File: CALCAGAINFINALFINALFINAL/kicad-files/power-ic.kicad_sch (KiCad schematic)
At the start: 18 parts, among them J2 USB_C_Receptacle_USB2.0_16P, SW10 SW_SPST, U5 TP4056-42-ESOP8, U6 TLV61070ADBV

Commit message: added 11pin expansion for accessories and micro-sd card slot
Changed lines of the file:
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@@
-		)
-	)
-	(label "VCC"
-		(at 77.216 62.23 0)
-		(effects
-			(font
-				(size 1.27 1.27)
-			)
-			(justify left bottom)
 		)
 	)
@@
 				(hide yes)
 			)
+		)
+	)
+	(global_label "VCC"
+		(shape input)
+		(at 77.216 62.23 0)
+		(fields_autoplaced yes)
+		(effects
+			(font
+				(size 1.27 1.27)
+			)
+			(justify left)
+		)
+		(property "Intersheetrefs" "${INTERSHEET_REFS}"
+			(at 83.8298 62.23 0)
+			(effects
+				(font
+					(size 1.27 1.27)
+				)
+				(justify left)
+				(hide yes)
+			)

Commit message: Finished SD card and screen. Added camera connector and adjacent gpio expander
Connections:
- net GND: now also J2.S1 (SHIELD)
- no-connect marks 3 -> 2
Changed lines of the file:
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@@
 		(at 77.216 90.17)
-	)
-	(no_connect
-		(at 54.356 100.33)
 	)
 	(wire
@@
 			(effects
 				(font
+					(size 1.27 1.27)
+				)
+				(justify right)
+				(hide yes)
+			)
+		)
+	)
+	(global_label "GND"
+		(shape input)
+		(at 54.356 100.33 270)
+		(fields_autoplaced yes)
+		(effects
+			(font
+				(size 1.27 1.27)
+			)
+			(justify right)
+		)
+		(property "Intersheetrefs" "${INTERSHEET_REFS}"
+			(at 54.356 107.1857 90)
+			(effects
+				(font

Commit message: nearly finished with the no camera variant schematic stil have 2 drc warnings to fix but should be done in the next few hours.
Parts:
- removed BT2: BAT, symbol Device:Battery_Cell
- added H6, H7: MountingHole_Pad, MountingHole:MountingHole_2.7mm_M2.5_ISO7380_Pad, symbol Mechanical:MountingHole_Pad
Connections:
- net BAT+: now also H7.1
- net GND: now also J2.SH (SHIELD), H6.1; no longer J2.S1 (SHIELD)

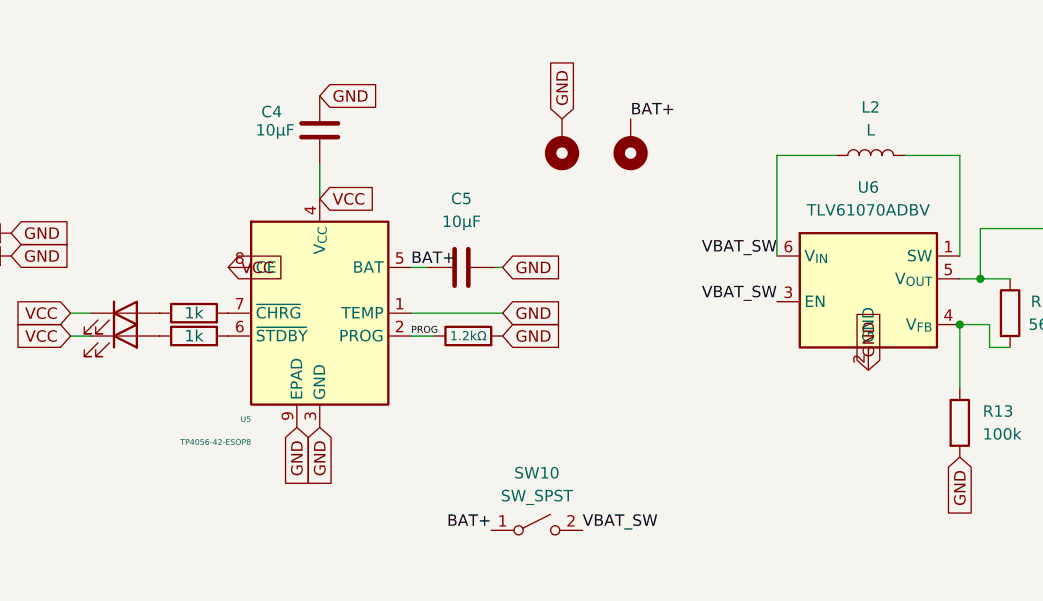
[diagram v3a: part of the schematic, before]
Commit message: finalised no-camera branch. designing pcb then committing to origin/no-camera then tracing and adding camera to main
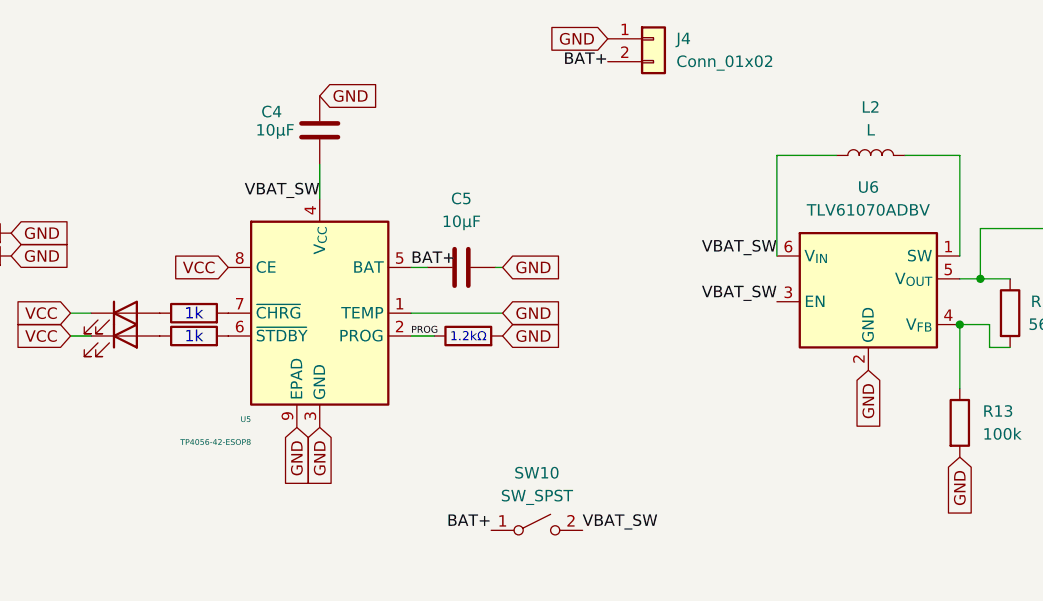
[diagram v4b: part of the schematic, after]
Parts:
- removed H6, H7: MountingHole_Pad, MountingHole:MountingHole_2.7mm_M2.5_ISO7380_Pad, symbol Mechanical:MountingHole_Pad
- added J4: Conn_01x02, Connector_JST:JST_XH_S2B-XH-A-1_1x02_P2.50mm_Horizontal, symbol Connector_Generic:Conn_01x02
- C4, C5, C6: footprint (none) -> Capacitor_SMD:CP_Elec_3x5.3
- D15, D20: footprint (none) -> LED_SMD:LED_Wurth_150044M155260
- L2: footprint (none) -> Inductor_SMD:L_6.3x6.3_H3
- R10, R11, R13, R14: footprint (none) -> Resistor_SMD:R_0201_0603Metric
- SW10: footprint (none) -> Button_Switch_SMD:SW_SPST_B3S-1000
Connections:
- net BAT+: now also J4.2 (Pin_2)
- net GND: now also J4.1 (Pin_1)
- net VBAT_SW: now also C4.2, U5.4 (V_{CC})
- net VCC: no longer C4.2, U5.4 (V_{CC})

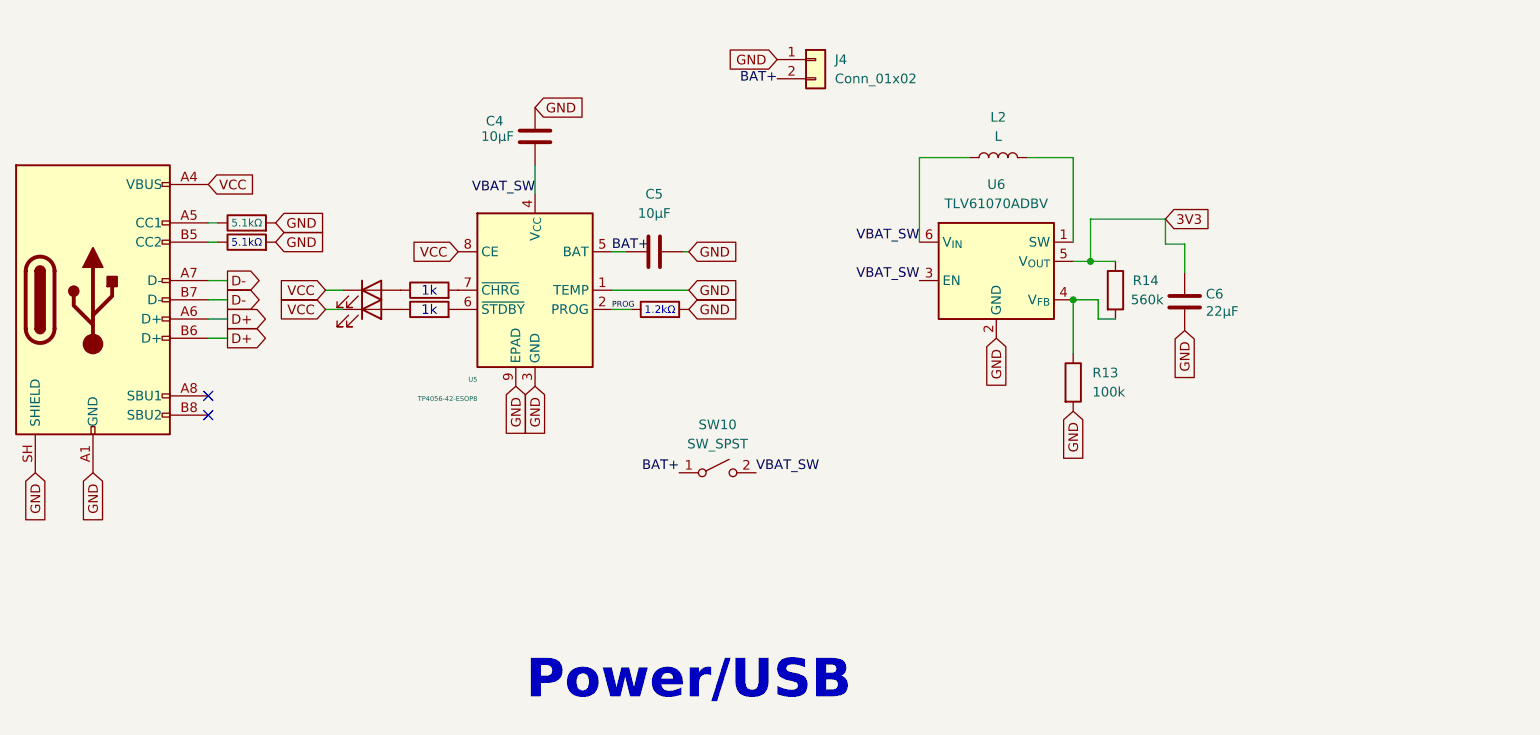
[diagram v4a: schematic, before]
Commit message: created initial pcb- need to do data and keypad tracing. finished power updated 3d models
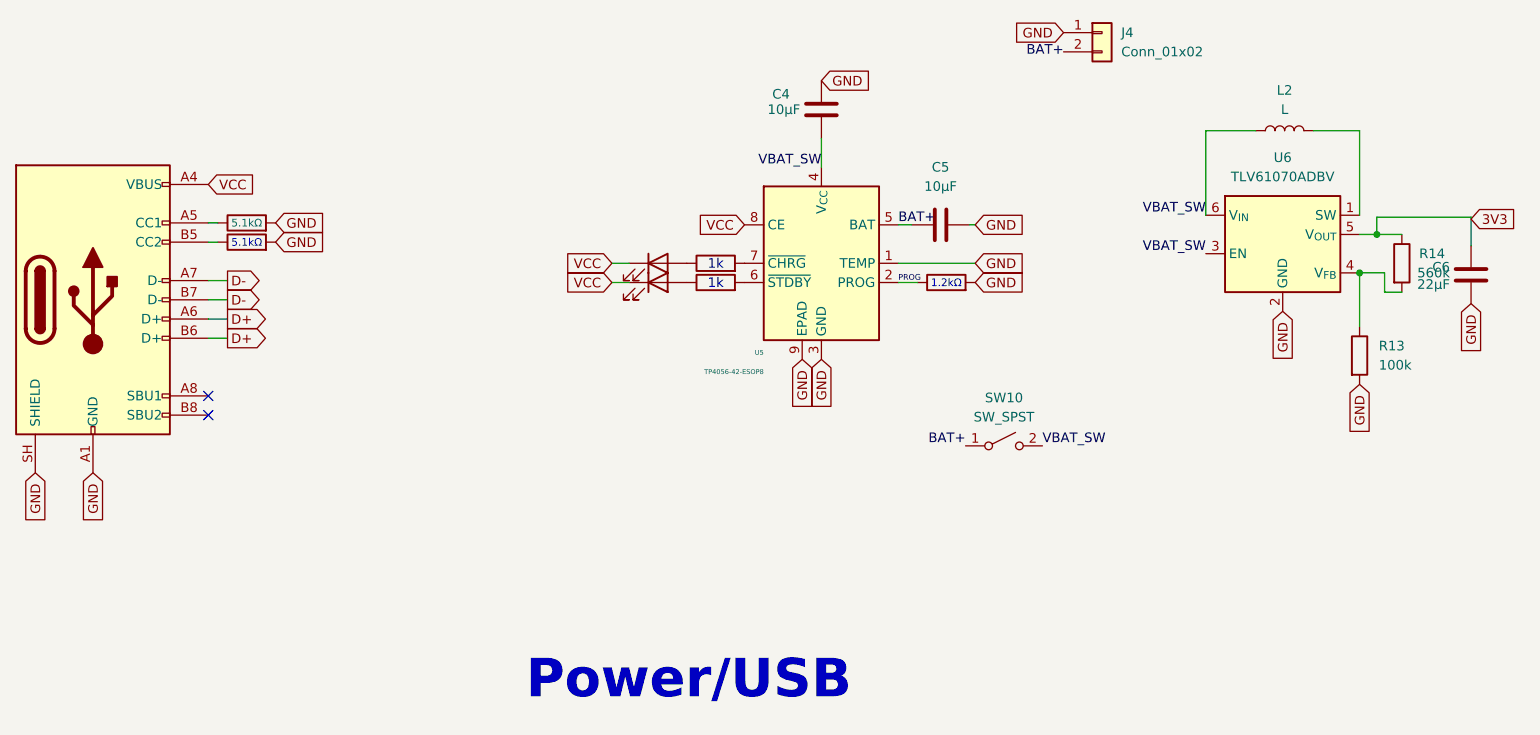
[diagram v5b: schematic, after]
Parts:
- D15, D20: footprint LED_SMD:LED_Wurth_150044M155260 -> LED_SMD:LED_01005_0402Metric
- SW10: footprint Button_Switch_SMD:SW_SPST_B3S-1000 -> Button_Switch_SMD:SW_DIP_SPSTx01_Slide_6.7x4.1mm_W6.73mm_P2.54mm_LowProfile_JPin
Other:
- moved on the sheet: C4, C5, C6, J4, L2, R13, R14, SW10, U5, U6

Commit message: dude this bitch ass project is the fucking boulder of sisyphus omfg ima genuinely kms at this rate if this iteration doesnt work ima genuinely kms like acutal this one is bare esp32 s3 with a diy antenna and crystal like dude what the actual fuck man ima genuinely dei. FINAL FINAL FINAL FINAL ITS GOT THE FUCKING BARE CHIPS FOR DAMN NEAR EVERYTHING DEAR MASS PRODUCED CHINK FACTORY GODS LET THIS THROUGH WITHOUT CAUSING A RUCKUS AND CHARGING LIKE $90 FOR 14 BUCKS OF PARTS AMEN
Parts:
- added R4, R5: 4k7R, symbol Device:R
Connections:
- net D+: now also R4.2; no longer J2.A6 (D+), J2.B6 (D+)
- net D-: now also R5.2; no longer J2.A7 (D-), J2.B7 (D-)
- new net: J2.A6 (D+), J2.B6 (D+), R4.1
- new net: J2.A7 (D-), J2.B7 (D-), R5.1
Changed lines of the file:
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@@
+	)
+	(junction
+		(at 77.216 82.55)
+		(diameter 0)
+		(color 0 0 0 0)
 	)
 	(junction
@@
 	)
 	(junction
+		(at 77.216 77.47)
+		(diameter 0)
+		(color 0 0 0 0)
+	)
+	(junction
 		(at 229.362 73.914)
 		(diameter 0)
@@
 	(wire
 		(pts
+			(xy 77.216 82.55) (xy 77.216 80.01)
+		)
+		(stroke
+			(width 0)
+			(type default)
+		)
+	)
+	(wire
+		(pts
 			(xy 209.042 55.118) (xy 215.646 55.118)
 		)
@@
 	(wire
 		(pts
-			(xy 79.756 77.47) (xy 77.216 77.47)
-		)
-		(stroke
-			(width 0)
-			(type default)
-		)
-	)
-	(wire
-		(pts
-			(xy 79.756 80.01) (xy 77.216 80.01)
+			(xy 98.044 77.47) (xy 91.948 77.47)
+		)
+		(stroke
+			(width 0)
+			(type default)
+		)
+	)
+	(wire
+		(pts
+			(xy 98.044 82.55) (xy 91.948 82.55)
+		)
+		(stroke
+			(width 0)
+			(type default)
+		)
+	)
+	(wire
+		(pts
+			(xy 77.216 82.55) (xy 84.328 82.55)
 		)
 		(stroke
@@
 	(wire
 		(pts
-			(xy 77.216 74.93) (xy 79.756 74.93)
-		)
-		(stroke
-			(width 0)
-			(type default)
-		)
-	)
-	(wire
-		(pts
 			(xy 158.242 56.134) (xy 158.242 59.944)
 		)
@@
 	(wire
 		(pts
+			(xy 77.216 74.93) (xy 77.216 77.47)
+		)
+		(stroke
+			(width 0)
+			(type default)
+		)
+	)
+	(wire
+		(pts
 			(xy 130.556 72.644) (xy 132.842 72.644)
 		)
@@
 	(wire
 		(pts
-			(xy 79.756 82.55) (xy 77.216 82.55)
+			(xy 84.328 77.47) (xy 77.216 77.47)
 		)
 		(stroke
@@
 	(global_label "D+"
 		(shape output)
-		(at 79.756 80.01 0)
+		(at 98.044 82.55 0)
 		(effects
 			(font
@@
 		)
 		(property "Intersheetrefs" "${INTERSHEET_REFS}"
-			(at 79.756 80.01 0)
+			(at 98.044 82.55 0)
 			(hide yes)
 			(show_name no)
@@
 		)
 	)
-	(global_label "D+"
-		(shape output)
-		(at 79.756 82.55 0)
-		(effects
-			(font
-				(size 1.27 1.27)
-			)
-			(justify left)
-		)
-		(property "Intersheetrefs" "${INTERSHEET_REFS}"
-			(at 79.756 82.55 0)
-			(hide yes)
-			(show_name no)
-			(do_not_autoplace no)
-			(effects
-				(font
-					(size 1.27 1.27)
-				)
-			)
-		)
-	)
 	(global_label "GND"
 		(shape input)
@@
 		)
 	)
-	(global_label "D-"
-		(shape output)
-		(at 79.756 74.93 0)
-		(effects
-			(font
-				(size 1.27 1.27)
-			)
-			(justify left)
-		)
-		(property "Intersheetrefs" "${INTERSHEET_REFS}"
-			(at 79.756 74.93 0)
-			(hide yes)
-			(show_name no)
-			(do_not_autoplace no)
-			(effects
-				(font
-					(size 1.27 1.27)
-				)
-			)
-		)
-	)
 	(global_label "GND"
 		(shape input)
@@
 	(global_label "D-"
 		(shape output)
-		(at 79.756 77.47 0)
+		(at 98.044 77.47 0)
 		(effects
 			(font
@@
 		)
 		(property "Intersheetrefs" "${INTERSHEET_REFS}"
-			(at 79.756 77.47 0)
+			(at 98.044 77.47 0)
 			(hide yes)
 			(show_name no)
@@
 	)
 	(symbol
+		(lib_id "Device:R")
+		(at 88.138 82.55 90)
+		(unit 1)
+		(body_style 1)
+		(exclude_from_sim no)
+		(in_bom yes)
+		(on_board yes)
+		(in_pos_files yes)
+		(dnp no)
+		(property "Reference" "R4"
+			(at 88.138 76.2 90)
+			(show_name no)
+			(do_not_autoplace no)
+			(effects
+				(font
+					(size 1.27 1.27)
+				)
+			)
+		)
+		(property "Value" "4k7R"
+			(at 88.138 82.55 90)
+			(show_name no)
+			(do_not_autoplace no)
+			(effects
+				(font
+					(size 1.27 1.27)
+				)
+			)
+		)
+		(property "Footprint" ""
+			(at 88.138 84.328 90)
+			(hide yes)
+			(show_name no)
+			(do_not_autoplace no)
+			(effects
+				(font
+					(size 1.27 1.27)
+				)
+			)
+		)
+		(property "Datasheet" ""
+			(at 88.138 82.55 0)
+			(hide yes)
+			(show_name no)
+			(do_not_autoplace no)
+			(effects
+				(font
+					(size 1.27 1.27)
+				)
+			)
+		)
+		(property "Description" "Resistor"
+			(at 88.138 82.55 0)
+			(hide yes)
+			(show_name no)
+			(do_not_autoplace no)
+			(effects
+				(font
+					(size 1.27 1.27)
+				)
+			)
+		)
+		(pin "1"
+		)
+		(pin "2"
+		)
+		(instances
+			(project "Cfx-port"
+				(path "/2a954a11-6412-4ea5-a14b-9a2b1d8affbf/37feafbc-0c2c-41fc-9817-e2aecf519d1e"
+					(reference "R4")
+					(unit 1)
+				)
+			)
+		)
+	)
+	(symbol
 		(lib_id "Device:LED")
 		(at 136.652 75.184 0)
@@
 					(unit 1)
 				)
+			)
+		)
+	)
+	(symbol
+		(lib_id "Device:R")
+		(at 88.138 77.47 90)
+		(unit 1)
+		(body_style 1)
+		(exclude_from_sim no)
+		(in_bom yes)
+		(on_board yes)
+		(in_pos_files yes)
+		(dnp no)
+		(property "Reference" "R5"
+			(at 88.138 71.12 90)
+			(show_name no)
+			(do_not_autoplace no)
+			(effects
+				(font
+					(size 1.27 1.27)
+				)
+			)
+		)
+		(property "Value" "4k7R"
+			(at 88.138 77.47 90)
+			(show_name no)
+			(do_not_autoplace no)
+			(effects
+				(font
+					(size 1.27 1.27)
+				)
+			)
+		)
+		(property "Footprint" ""
+			(at 88.138 79.248 90)
+			(hide yes)
+			(show_name no)
+			(do_not_autoplace no)
+			(effects
+				(font
+					(size 1.27 1.27)
+				)
+			)
+		)
+		(property "Datasheet" ""
+			(at 88.138 77.47 0)
+			(hide yes)
+			(show_name no)
+			(do_not_autoplace no)
+			(effects
+				(font
+					(size 1.27 1.27)
+				)
+			)
+		)
+		(property "Description" "Resistor"
+			(at 88.138 77.47 0)
+			(hide yes)
+			(show_name no)
+			(do_not_autoplace no)
+			(effects
+				(font
+					(size 1.27 1.27)
+				)
+			)
+		)
+		(pin "1"
+		)
+		(pin "2"
+		)
+		(instances
+			(project "Cfx-port"
+				(path "/2a954a11-6412-4ea5-a14b-9a2b1d8affbf/37feafbc-0c2c-41fc-9817-e2aecf519d1e"
+					(reference "R5")
+					(unit 1)
+				)

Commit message: finalised pcb w camera. thing is im kinda poor rn and ill prob get enough money to order pcba after 2 weeks. until then ima js focus on school and get thru to working on tweaking the HAL and ui to match my spec and the design language of ABSOLUT-CAS
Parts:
- C4, C5: footprint Capacitor_SMD:CP_Elec_3x5.3 -> Capacitor_SMD:C_0603_1608Metric; KiLib_Generator (none) -> SMD_2terminal_chip_molded; LCSC (none) -> C7171
- C6: footprint Capacitor_SMD:CP_Elec_3x5.3 -> Capacitor_SMD:C_0603_1608Metric; KiLib_Generator (none) -> SMD_2terminal_chip_molded; LCSC (none) -> C5672
- D15: KiLib_Generator (none) -> SMD_2terminal_chip_molded; LCSC (none) -> C2286
- J2: LCSC (none) -> C52989302
- J4: KiLib_Generator (none) -> connector/JST
- L2: LCSC (none) -> C1035
- R10, R11: KiLib_Generator (none) -> SMD_2terminal_chip_molded; LCSC (none) -> C4410
- R12: value R -> 1.2; KiLib_Generator (none) -> SMD_2terminal_chip_molded; LCSC (none) -> C17379
- R13: KiLib_Generator (none) -> SMD_2terminal_chip_molded; LCSC (none) -> C17900
- R14: KiLib_Generator (none) -> SMD_2terminal_chip_molded; LCSC (none) -> C23203
- R8: value 5.1kΩ -> 5.1k; KiLib_Generator (none) -> SMD_2terminal_chip_molded; LCSC (none) -> C23186
- R9: value R -> 5.1k; KiLib_Generator (none) -> SMD_2terminal_chip_molded; LCSC (none) -> C23186
- U5: KiLib_Generator (none) -> package/gullwing; LCSC (none) -> C16581
- U6: KiLib_Generator (none) -> package/gullwing; LCSC (none) -> C6881375
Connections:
- net BAT+: now also C4.2, L2.1, U5.4 (V_{CC}), U6.3 (EN), U6.6 (V_{IN})
- net VBAT_SW: no longer C4.2, L2.1, U5.4 (V_{CC}), U6.3 (EN), U6.6 (V_{IN})
- net usb_P: now reaches J2.A6 (D+), J2.B6 (D+), R4.1
- net usb_N: now reaches J2.A7 (D-), J2.B7 (D-), R5.1

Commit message: hgjfhgjfhgfjghfjghf
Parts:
- removed SW10: SW_SPST, Button_Switch_SMD:SW_DIP_SPSTx01_Slide_6.7x4.1mm_W6.73mm_P2.54mm_LowProfile_JPin, symbol Switch:SW_SPST
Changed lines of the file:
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@@
-		)
-	)
-	(label "VBAT_SW"
-		(at 187.452 96.774 0)
-		(effects
-			(font
-				(size 1.27 1.27)
-			)
-			(justify left bottom)
 		)
 	)
@@
 			)
 			(justify left bottom)
-		)
-	)
-	(label "BAT+"
-		(at 177.292 96.774 180)
-		(effects
-			(font
-				(size 1.27 1.27)
-			)
-			(justify right bottom)
 		)
 	)
@@
 					)
 				)
-			)
-		)
-	)
-	(symbol
-		(lib_id "Switch:SW_SPST")
-		(at 182.372 96.774 0)
-		(unit 1)
-		(body_style 1)
-		(exclude_from_sim no)
-		(in_bom yes)
-		(on_board yes)
-		(in_pos_files yes)
-		(dnp no)
-		(property "Reference" "SW10"
-			(at 182.372 90.424 0)
-			(show_name no)
-			(do_not_autoplace no)
-			(effects
-				(font
-					(size 1.27 1.27)
-				)
-			)
-		)
-		(property "Value" "SW_SPST"
-			(at 182.372 92.964 0)
-			(show_name no)
-			(do_not_autoplace no)
-			(effects
-				(font
-					(size 1.27 1.27)
-				)
-			)
-		)
-		(property "Footprint" "Button_Switch_SMD:SW_DIP_SPSTx01_Slide_6.7x4.1mm_W6.73mm_P2.54mm_LowProfile_JPin"
-			(at 182.372 96.774 0)
-			(hide yes)
-			(show_name no)
-			(do_not_autoplace no)
-			(effects
-				(font
-					(size 1.27 1.27)
-				)
-			)
-		)
-		(property "Datasheet" ""
-			(at 182.372 96.774 0)
-			(hide yes)
-			(show_name no)
-			(do_not_autoplace no)
-			(effects
-				(font
-					(size 1.27 1.27)
-				)
-			)
-		)
-		(property "Description" "Single Pole Single Throw (SPST) switch"
-			(at 182.372 96.774 0)
-			(hide yes)
-			(show_name no)
-			(do_not_autoplace no)
-			(effects
-				(font
-					(size 1.27 1.27)
-				)
-			)
-		)
-		(pin "2"
-		)
-		(pin "1"
-		)
-		(instances
-			(project "Cfx-port"
-				(path "/2a954a11-6412-4ea5-a14b-9a2b1d8affbf/37feafbc-0c2c-41fc-9817-e2aecf519d1e"
-					(reference "SW10")
-					(unit 1)
-					(variant
-						(name "goody2shoes-nocamera")
-						(in_bom no)
-						(field
-							(name "Footprint")
-							(value "Button_Switch_SMD:SW_SPST_REED_CT05-XXXX-J1")
-						)
-					)
-				)
